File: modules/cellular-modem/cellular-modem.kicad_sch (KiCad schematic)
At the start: 23 parts, among them J1 MM60-mini-PCIe, J2 MM60-EZH059-B5-R650, U1 TXV0108RGYR, U2 TXV0108RGYR, U3 TXV0108RGYR, U4 TPS631000DRLR, U5 TPS631000DRLR

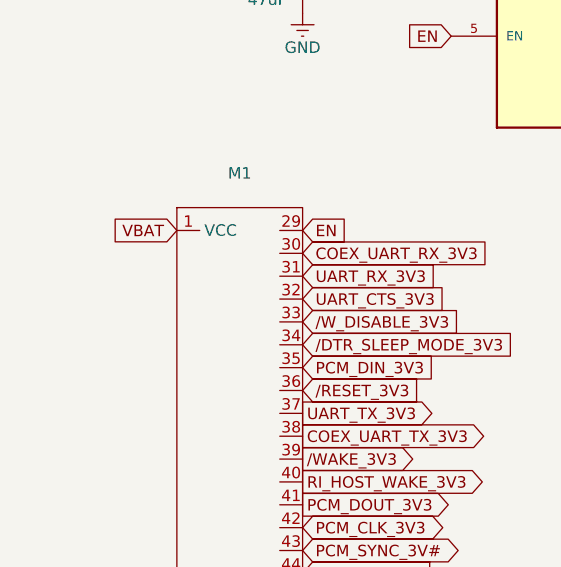
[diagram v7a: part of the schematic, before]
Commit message: label all pads
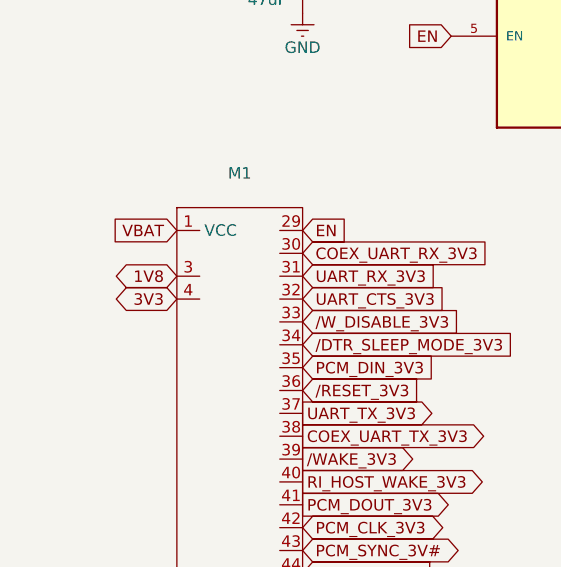
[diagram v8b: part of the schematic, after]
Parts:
- removed M1: ~, MegaCastle:MegaCastle2x28-Module-I36.0x66.3-M800007FFFFFFFF-NIBBLE, symbol MegaCastle:MegaCastle2x28-Module-I36.0x66.3-M800007FFFFFFFF-NOCUTOUT
- added M1: ~, MegaCastle:MegaCastle2x28-Module-I36.0x66.3-MB00007FFFFFFFF-NIBBLE, symbol MegaCastle:MegaCastle2x28-Module-I36.0x66.3-MB00007FFFFFFFF-NOCUTOUT
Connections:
- net 1V8: now also M1.3
- net 3V3: now also M1.4
- net COEX_UART_RX_3V3: now also M1.30
- net COEX_UART_TX_3V3: now also M1.38
- net EN: now also M1.29
- net GND: now also M1.28 (GND)
- net I2C_DATA_1V8: now also M1.52
- net I2C_SCL_1V8: now also M1.53
- net PCM_CLK_3V3: now also M1.42
- net PCM_CLK_DIR: now also M1.44
- net PCM_DIN_3V3: now also M1.35
- net PCM_DOUT_3V3: now also M1.41
- net PCM_SYNC_3V#: now also M1.43
- net PERp0: now also M1.55
- net PETp0: now also M1.54
- net RESERVED_PIN19: now also M1.56
- net RESERVED_PIN46: now also M1.49
- net RI_HOST_WAKE_3V3: now also M1.40
- net UART_CTS_3V3: now also M1.32
- net UART_RX_3V3: now also M1.31
- net UART_TX_3V3: now also M1.37
- net USB_D+: now also M1.48
- net USB_D-: now also M1.47
- net USIM_CLK: now also M1.24
- net USIM_DATA: now also M1.23
- net USIM_SIM_PRESENT_IN: now also M1.50
- net USIM_VDD: now also M1.22
- net USIM_VPP: now also M1.26
- net VBAT: now also M1.1 (VCC)
- net /CLKREQ: now also M1.27
- net /DTR_SLEEP_MODE_3V3: now also M1.34
- net /LED_WWAN_OC_OUT: now also M1.51
- net /RESET_3V3: now also M1.36
- net /USIM_RESET: now also M1.25
- net /WAKE_3V3: now also M1.39
- net /W_DISABLE_3V3: now also M1.33
